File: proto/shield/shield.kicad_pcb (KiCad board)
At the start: 2 copper layers, 69.8 x 132.7 mm, 124 parts, among them J1 ESC_XY, J10 gpio_d, J11 gpio_d, J12 gpio_d, J13 gpio_d, J14 gpio_a, J15 gpio_a, J16 gpio_a, J17 gpio_a, J18 gpio_a, J19 gpio_a, J2 ESC_4Z, J20 gpio_a, J21 gpio_a, J22 5V_IN_A, J23 5V_IN_D, J24 CAN_LINK, J25 Conn_01x04, J3 PWM1, J4 PWM2, J5 PWM3, J6 gpio_d, J7 gpio_d, J8 gpio_d, J9 gpio_d, U1 NUCLEO144-F767ZI, U10 LTV-817S, U11 LTV-817S, U12 LTV-817S, U13 LTV-817S, U14 LTV-817S, U15 LTV-817S, U16 LTV-817S, U17 LTV-817S, U18 SN65HVD230, U19 MAX3232, U2 6N137, U3 6N137, U4 6N137, U5 6N137, U6 6N137, U7 6N137, U8 6N137, U9 6N137

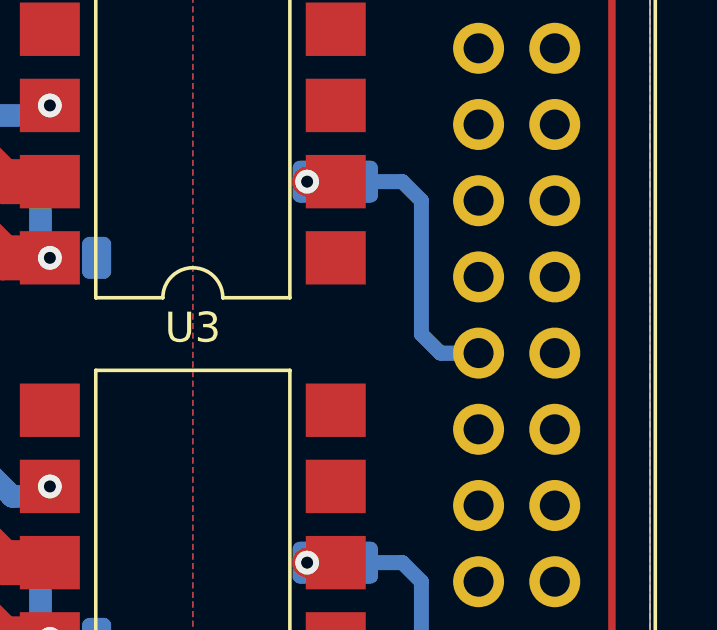
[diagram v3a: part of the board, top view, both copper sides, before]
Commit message: pa5->pa6
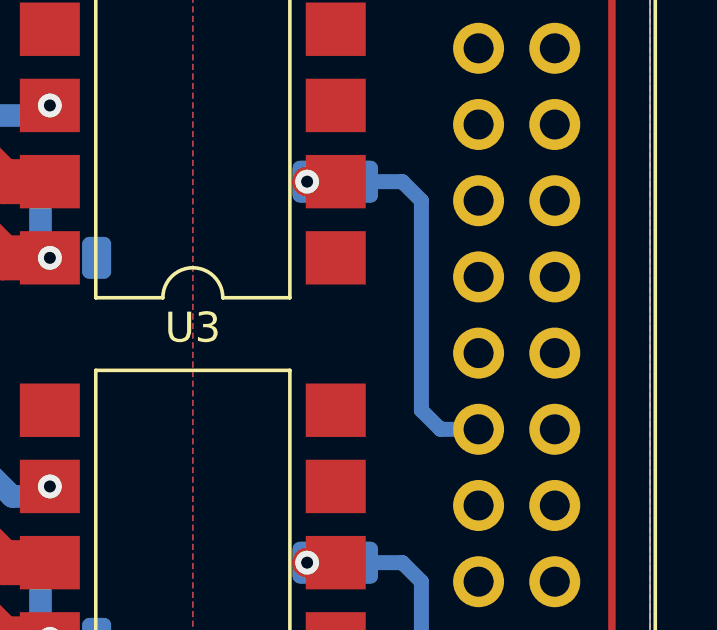
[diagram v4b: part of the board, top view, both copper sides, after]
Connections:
- U1 pad 83: /TIM3_CH2 -> (no net)
- U1 pad 85: (no net) -> /TIM3_CH2
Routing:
- net /TIM3_CH2: track 8.81 -> 11.4 mm
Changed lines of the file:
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@@
   )
   (setup
-    (last_trace_width 0.75)
+    (last_trace_width 0.25)
     (user_trace_width 0.5)
     (user_trace_width 0.75)
@@
     (add_net "Net-(R5-Pad1)")
     (add_net "Net-(R55-Pad1)")
+    (add_net "Net-(U1-Pad1)")
+    (add_net "Net-(U1-Pad10)")
+    (add_net "Net-(U1-Pad100)")
+    (add_net "Net-(U1-Pad101)")
+    (add_net "Net-(U1-Pad102)")
+    (add_net "Net-(U1-Pad103)")
+    (add_net "Net-(U1-Pad104)")
+    (add_net "Net-(U1-Pad105)")
+    (add_net "Net-(U1-Pad106)")
+    (add_net "Net-(U1-Pad107)")
+    (add_net "Net-(U1-Pad108)")
+    (add_net "Net-(U1-Pad109)")
+    (add_net "Net-(U1-Pad11)")
+    (add_net "Net-(U1-Pad110)")
+    (add_net "Net-(U1-Pad112)")
+    (add_net "Net-(U1-Pad114)")
+    (add_net "Net-(U1-Pad116)")
+    (add_net "Net-(U1-Pad117)")
+    (add_net "Net-(U1-Pad119)")
+    (add_net "Net-(U1-Pad12)")
+    (add_net "Net-(U1-Pad121)")
+    (add_net "Net-(U1-Pad122)")
+    (add_net "Net-(U1-Pad123)")
+    (add_net "Net-(U1-Pad124)")
+    (add_net "Net-(U1-Pad125)")
+    (add_net "Net-(U1-Pad127)")
+    (add_net "Net-(U1-Pad128)")
+    (add_net "Net-(U1-Pad129)")
+    (add_net "Net-(U1-Pad13)")
+    (add_net "Net-(U1-Pad130)")
+    (add_net "Net-(U1-Pad131)")
+    (add_net "Net-(U1-Pad132)")
+    (add_net "Net-(U1-Pad133)")
+    (add_net "Net-(U1-Pad134)")
+    (add_net "Net-(U1-Pad137)")
+    (add_net "Net-(U1-Pad138)")
+    (add_net "Net-(U1-Pad139)")
+    (add_net "Net-(U1-Pad14)")
+    (add_net "Net-(U1-Pad140)")
+    (add_net "Net-(U1-Pad141)")
+    (add_net "Net-(U1-Pad142)")
+    (add_net "Net-(U1-Pad15)")
+    (add_net "Net-(U1-Pad17)")
+    (add_net "Net-(U1-Pad2)")
+    (add_net "Net-(U1-Pad21)")
+    (add_net "Net-(U1-Pad23)")
+    (add_net "Net-(U1-Pad24)")
+    (add_net "Net-(U1-Pad25)")
+    (add_net "Net-(U1-Pad26)")
+    (add_net "Net-(U1-Pad27)")
+    (add_net "Net-(U1-Pad28)")
+    (add_net "Net-(U1-Pad29)")
+    (add_net "Net-(U1-Pad3)")
+    (add_net "Net-(U1-Pad30)")
+    (add_net "Net-(U1-Pad31)")
+    (add_net "Net-(U1-Pad32)")
+    (add_net "Net-(U1-Pad33)")
+    (add_net "Net-(U1-Pad34)")
+    (add_net "Net-(U1-Pad36)")
+    (add_net "Net-(U1-Pad38)")
+    (add_net "Net-(U1-Pad48)")
+    (add_net "Net-(U1-Pad5)")
+    (add_net "Net-(U1-Pad50)")
+    (add_net "Net-(U1-Pad51)")
+    (add_net "Net-(U1-Pad52)")
+    (add_net "Net-(U1-Pad53)")
+    (add_net "Net-(U1-Pad54)")
+    (add_net "Net-(U1-Pad56)")
+    (add_net "Net-(U1-Pad58)")
+    (add_net "Net-(U1-Pad59)")
+    (add_net "Net-(U1-Pad62)")
+    (add_net "Net-(U1-Pad63)")
+    (add_net "Net-(U1-Pad64)")
+    (add_net "Net-(U1-Pad65)")
+    (add_net "Net-(U1-Pad66)")
+    (add_net "Net-(U1-Pad67)")
+    (add_net "Net-(U1-Pad68)")
+    (add_net "Net-(U1-Pad69)")
+    (add_net "Net-(U1-Pad7)")
+    (add_net "Net-(U1-Pad70)")
+    (add_net "Net-(U1-Pad73)")
+    (add_net "Net-(U1-Pad75)")
+    (add_net "Net-(U1-Pad76)")
+    (add_net "Net-(U1-Pad77)")
+    (add_net "Net-(U1-Pad78)")
+    (add_net "Net-(U1-Pad79)")
+    (add_net "Net-(U1-Pad80)")
+    (add_net "Net-(U1-Pad82)")
+    (add_net "Net-(U1-Pad83)")
+    (add_net "Net-(U1-Pad84)")
+    (add_net "Net-(U1-Pad86)")
+    (add_net "Net-(U1-Pad87)")
+    (add_net "Net-(U1-Pad88)")
+    (add_net "Net-(U1-Pad89)")
+    (add_net "Net-(U1-Pad9)")
+    (add_net "Net-(U1-Pad90)")
+    (add_net "Net-(U1-Pad93)")
+    (add_net "Net-(U1-Pad94)")
+    (add_net "Net-(U1-Pad95)")
+    (add_net "Net-(U1-Pad97)")
+    (add_net "Net-(U1-Pad98)")
+    (add_net "Net-(U1-Pad99)")
+    (add_net "Net-(U18-Pad5)")
+    (add_net "Net-(U19-Pad10)")
+    (add_net "Net-(U19-Pad7)")
+    (add_net "Net-(U19-Pad8)")
+    (add_net "Net-(U19-Pad9)")
+    (add_net "Net-(U2-Pad1)")
+    (add_net "Net-(U3-Pad1)")
+    (add_net "Net-(U4-Pad1)")
+    (add_net "Net-(U5-Pad1)")
+    (add_net "Net-(U6-Pad1)")
+    (add_net "Net-(U7-Pad1)")
+    (add_net "Net-(U8-Pad1)")
+    (add_net "Net-(U9-Pad1)")
   )
   (module Module:ST_Morpho_Connector_144_STLink (layer F.Cu)
@@
     (pad 87 thru_hole circle (at 60.96 17.78) (size 1.7 1.7) (drill 1) (layers *.Cu *.Mask))
     (pad 86 thru_hole circle (at 63.5 15.24) (size 1.7 1.7) (drill 1) (layers *.Cu *.Mask))
-    (pad 85 thru_hole circle (at 60.96 15.24) (size 1.7 1.7) (drill 1) (layers *.Cu *.Mask))
-    (pad 84 thru_hole circle (at 63.5 12.7) (size 1.7 1.7) (drill 1) (layers *.Cu *.Mask))
-    (pad 83 thru_hole circle (at 60.96 12.7) (size 1.7 1.7) (drill 1) (layers *.Cu *.Mask)
+    (pad 85 thru_hole circle (at 60.96 15.24) (size 1.7 1.7) (drill 1) (layers *.Cu *.Mask)
       (net 29 /TIM3_CH2))
+    (pad 84 thru_hole circle (at 63.5 12.7) (size 1.7 1.7) (drill 1) (layers *.Cu *.Mask))
+    (pad 83 thru_hole circle (at 60.96 12.7) (size 1.7 1.7) (drill 1) (layers *.Cu *.Mask))
     (pad 82 thru_hole circle (at 63.5 10.16) (size 1.7 1.7) (drill 1) (layers *.Cu *.Mask))
     (pad 81 thru_hole circle (at 60.96 10.16) (size 1.7 1.7) (drill 1) (layers *.Cu *.Mask)
@@
   (via (at 98.425 65.405) (size 0.8) (drill 0.4) (layers F.Cu B.Cu) (net 28))
   (segment (start 99.38 65.405) (end 98.425 65.405) (width 1) (layer F.Cu) (net 28))
+  (segment (start 102.235 78.74) (end 102.235 85.725) (width 0.5) (layer B.Cu) (net 29))
+  (segment (start 102.87 86.36) (end 104.14 86.36) (width 0.5) (layer B.Cu) (net 29))
   (segment (start 100.3 78.105) (end 101.6 78.105) (width 0.5) (layer B.Cu) (net 29))
+  (segment (start 102.235 85.725) (end 102.87 86.36) (width 0.5) (layer B.Cu) (net 29))
   (segment (start 101.6 78.105) (end 102.235 78.74) (width 0.5) (layer B.Cu) (net 29))
-  (segment (start 102.235 78.74) (end 102.235 83.185) (width 0.5) (layer B.Cu) (net 29))
-  (segment (start 102.87 83.82) (end 104.14 83.82) (width 0.5) (layer B.Cu) (net 29))
-  (segment (start 102.235 83.185) (end 102.87 83.82) (width 0.5) (layer B.Cu) (net 29))
   (via (at 98.425 78.105) (size 0.8) (drill 0.4) (layers F.Cu B.Cu) (net 30))
   (segment (start 99.38 78.105) (end 98.425 78.105) (width 1) (layer F.Cu) (net 30))

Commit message: finall pcb
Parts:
- D6, D7: value LED_B -> PWR
- J10: value gpio_d -> IO5
- J11: value gpio_d -> IO6
- J12: value gpio_d -> IO7
- J13: value gpio_d -> IO8
- J14: value gpio_a -> IO1_A
- J15: value gpio_a -> IO2_A
- J16: value gpio_a -> IO3_A
- J17: value gpio_a -> IO4_A
- J18: value gpio_a -> IO5_A
- J19: value gpio_a -> IO6_A
- J20: value gpio_a -> IO7_A
- J21: value gpio_a -> IO8_A
- J24: value CAN_LINK -> CAN
- J25: value Conn_01x04 -> RS232
- J6: value gpio_d -> IO1
- J7: value gpio_d -> IO2
- J8: value gpio_d -> IO3
- J9: value gpio_d -> IO4
- renumbered R57 to CAN_R1, R55 to CAN_R2, R56 to CAN_R3
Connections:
- net /TIM3_CH1 renamed /PWM_T1_IN
- net /TIM3_CH1_A renamed /PWM_T1
- net /TIM3_CH2 renamed /PWM_T2_IN
- net /TIM3_CH2_A renamed /PWM_T2
- net /TIM3_CH3 renamed /PWM_T3_IN
- net /TIM3_CH3_A renamed /PWM_T3
- net /TIM3_CH4 renamed /PWM_T4_IN
- net /TIM3_CH4_A renamed /PWM_T4
- net /TIM4_CH1 renamed /PWM_T5:T8_IN
- net /TIM4_CH1_A renamed /PWM_T5:T8
- net /TIM4_CH2 renamed /PWM_OPT1_IN
- net /TIM4_CH2_A renamed /PWM_OPT1
- net /TIM4_CH3 renamed /PWM_OPT2_IN
- net /TIM4_CH3_A renamed /PWM_OPT2
- net /TIM4_CH4 renamed /PWM_OPT3_IN
- net /TIM4_CH4_A renamed /PWM_OPT3
